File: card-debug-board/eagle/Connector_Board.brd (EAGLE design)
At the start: 65.5 x 34.3 mm, 37 parts, among them J1 ORESAT-DEBUG-CONNECTOR-CARD, J3 USB_A_SMT_FEMALE, Q1 MOSFET-PCH-SOT23-6, U1 FT230XS-R

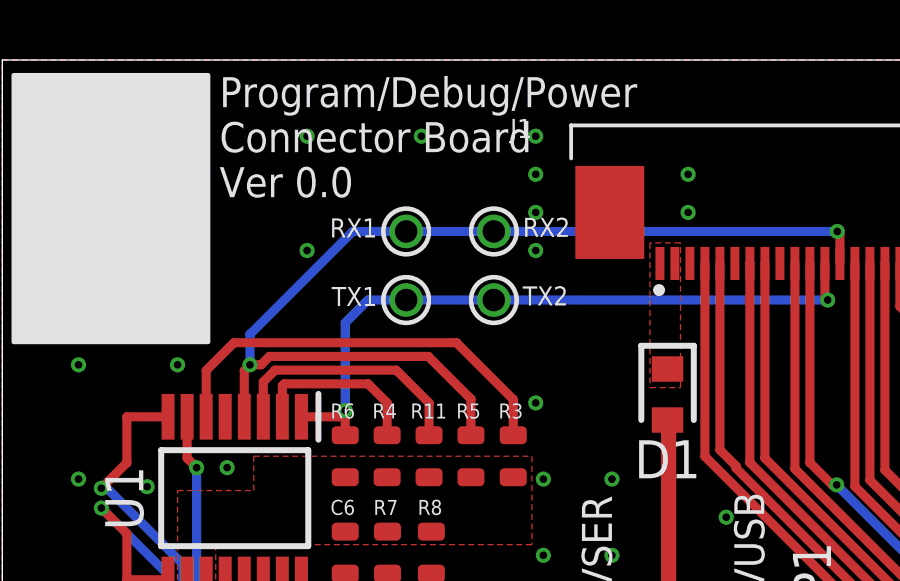
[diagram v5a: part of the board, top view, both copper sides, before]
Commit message: updated the pin connectors
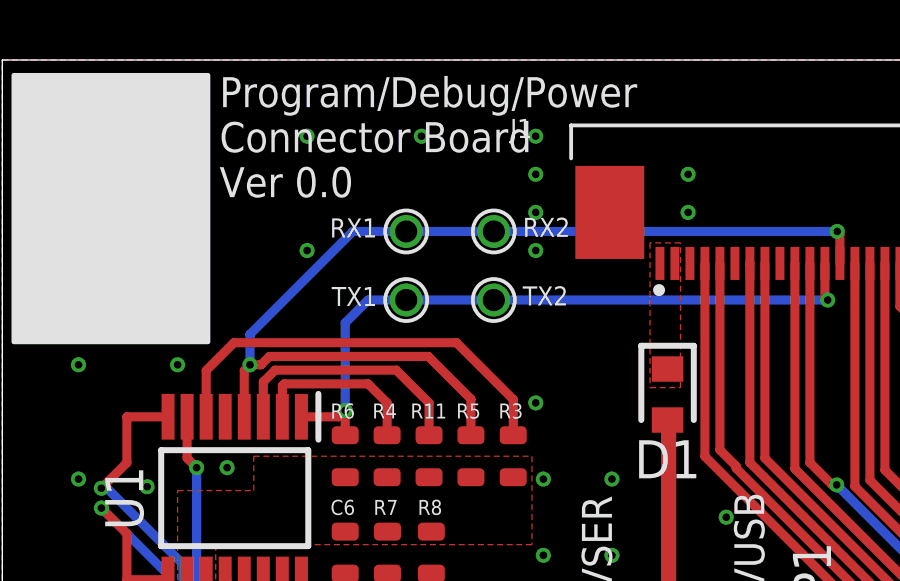
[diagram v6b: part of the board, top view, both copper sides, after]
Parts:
- RX1, RX2, TX1, TX2: value (none) -> TEST-POINT-LARGE; device oresat-misc:TP -> oresat-misc:1X01
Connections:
- net RXD: now also RX1.1, RX2.1; no longer RX1.TP, RX2.TP
- net TXD: now also TX1.1, TX2.1; no longer TX1.TP, TX2.TP
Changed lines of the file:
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@@
 <drawing>
 <settings>
-<setting alwaysvectorfont="yes"/>
+<setting alwaysvectorfont="no"/>
 <setting verticaltext="up"/>
 </settings>
@@
 <layer number="136" name="silktop" color="7" fill="1" visible="yes" active="yes"/>
 <layer number="137" name="silkbottom" color="7" fill="1" visible="yes" active="yes"/>
+<layer number="138" name="mbTest" color="7" fill="1" visible="yes" active="yes"/>
+<layer number="139" name="mtKeepout" color="7" fill="1" visible="yes" active="yes"/>
 <layer number="140" name="Testjig_Mill" color="26" fill="1" visible="yes" active="yes"/>
+<layer number="141" name="mtRestrict" color="7" fill="1" visible="yes" active="yes"/>
+<layer number="142" name="mbRestrict" color="7" fill="1" visible="yes" active="yes"/>
+<layer number="143" name="mvRestrict" color="7" fill="1" visible="yes" active="yes"/>
 <layer number="144" name="Drill_legend" color="7" fill="1" visible="yes" active="yes"/>
 <layer number="145" name="DrillLegend_01-16" color="7" fill="1" visible="yes" active="yes"/>
 <layer number="146" name="DrillLegend_01-20" color="7" fill="1" visible="yes" active="yes"/>
+<layer number="147" name="mMeasures" color="7" fill="1" visible="yes" active="yes"/>
+<layer number="148" name="mDocument" color="7" fill="1" visible="yes" active="yes"/>
+<layer number="149" name="mReference" color="7" fill="1" visible="yes" active="yes"/>
 <layer number="150" name="Notes" color="7" fill="1" visible="yes" active="yes"/>
 <layer number="151" name="HeatSink" color="7" fill="1" visible="yes" active="yes"/>
@@
 <layer number="154" name="FabDoc2" color="7" fill="1" visible="yes" active="yes"/>
 <layer number="155" name="FabDoc3" color="7" fill="1" visible="yes" active="yes"/>
+<layer number="191" name="mNets" color="7" fill="1" visible="yes" active="yes"/>
+<layer number="192" name="mBusses" color="7" fill="1" visible="yes" active="yes"/>
+<layer number="193" name="mPins" color="7" fill="1" visible="yes" active="yes"/>
+<layer number="194" name="mSymbols" color="7" fill="1" visible="yes" active="yes"/>
+<layer number="195" name="mNames" color="7" fill="1" visible="yes" active="yes"/>
+<layer number="196" name="mValues" color="7" fill="1" visible="yes" active="yes"/>
 <layer number="199" name="Contour" color="7" fill="1" visible="yes" active="yes"/>
 <layer number="200" name="200bmp" color="7" fill="1" visible="yes" active="yes"/>
@@
 <attribute name="VALUE" x="12.674" y="22.082" size="0.8" layer="27" font="vector" ratio="15" rot="R270"/>
 </element>
-<element name="RX1" library="oresat-misc" package="TP" package3d_urn="urn:adsk.eagle:package:27946/1" value="" x="13.462" y="28.575" smashed="yes">
+<element name="RX1" library="oresat-misc" package="1X01" value="TEST-POINT-LARGE" x="13.462" y="28.575" smashed="yes">
 <attribute name="NAME" x="12.496" y="29.01" size="0.635" layer="25" font="vector" ratio="20" rot="R180"/>
-<attribute name="POPULARITY" value="12" x="13.462" y="28.575" size="1" layer="27" display="off"/>
-<attribute name="VALUE" value="" x="13.462" y="28.575" size="0.0254" layer="27"/>
-</element>
-<element name="RX2" library="oresat-misc" package="TP" package3d_urn="urn:adsk.eagle:package:27946/1" value="" x="16.383" y="28.575" smashed="yes">
+</element>
+<element name="RX2" library="oresat-misc" package="1X01" value="TEST-POINT-LARGE" x="16.383" y="28.575" smashed="yes">
 <attribute name="NAME" x="17.349" y="28.394" size="0.635" layer="25" font="vector" ratio="20"/>
-<attribute name="POPULARITY" value="12" x="16.383" y="28.575" size="1" layer="27" display="off"/>
-<attribute name="VALUE" value="" x="16.383" y="28.575" size="0.0254" layer="27"/>
-</element>
-<element name="TX1" library="oresat-misc" package="TP" package3d_urn="urn:adsk.eagle:package:27946/1" value="" x="13.462" y="26.289" smashed="yes">
+</element>
+<element name="TX1" library="oresat-misc" package="1X01" value="TEST-POINT-LARGE" x="13.462" y="26.289" smashed="yes">
 <attribute name="NAME" x="12.496" y="26.724" size="0.635" layer="25" font="vector" ratio="20" rot="R180"/>
-<attribute name="POPULARITY" value="12" x="13.462" y="26.289" size="1" layer="27" display="off"/>
-<attribute name="VALUE" value="" x="13.462" y="26.289" size="0.0254" layer="27"/>
-</element>
-<element name="TX2" library="oresat-misc" package="TP" package3d_urn="urn:adsk.eagle:package:27946/1" value="" x="16.383" y="26.289" smashed="yes">
+</element>
+<element name="TX2" library="oresat-misc" package="1X01" value="TEST-POINT-LARGE" x="16.383" y="26.289" smashed="yes">
 <attribute name="NAME" x="17.349" y="26.108" size="0.635" layer="25" font="vector" ratio="20"/>
-<attribute name="POPULARITY" value="12" x="16.383" y="26.289" size="1" layer="27" display="off"/>
-<attribute name="VALUE" value="" x="16.383" y="26.289" size="0.0254" layer="27"/>
 </element>
 </elements>
@@
 <contactref element="U1" pad="1"/>
 <contactref element="R6" pad="1"/>
-<contactref element="TX1" pad="TP"/>
-<contactref element="TX2" pad="TP"/>
+<contactref element="TX1" pad="1"/>
+<contactref element="TX2" pad="1"/>
 <wire x1="9.969" y1="22.397" x2="11.221" y2="22.397" width="0.3048" layer="1"/>
 <wire x1="11.221" y1="22.397" x2="11.43" y2="22.606" width="0.3048" layer="1"/>
@@
 <contactref element="U1" pad="4"/>
 <contactref element="R5" pad="1"/>
-<contactref element="RX1" pad="TP"/>
-<contactref element="RX2" pad="TP"/>
+<contactref element="RX1" pad="1"/>
+<contactref element="RX2" pad="1"/>
 <wire x1="8.065" y1="22.397" x2="8.065" y2="23.94" width="0.3048" layer="1"/>
 <wire x1="8.065" y1="23.94" x2="8.255" y2="24.13" width="0.3048" layer="1"/>

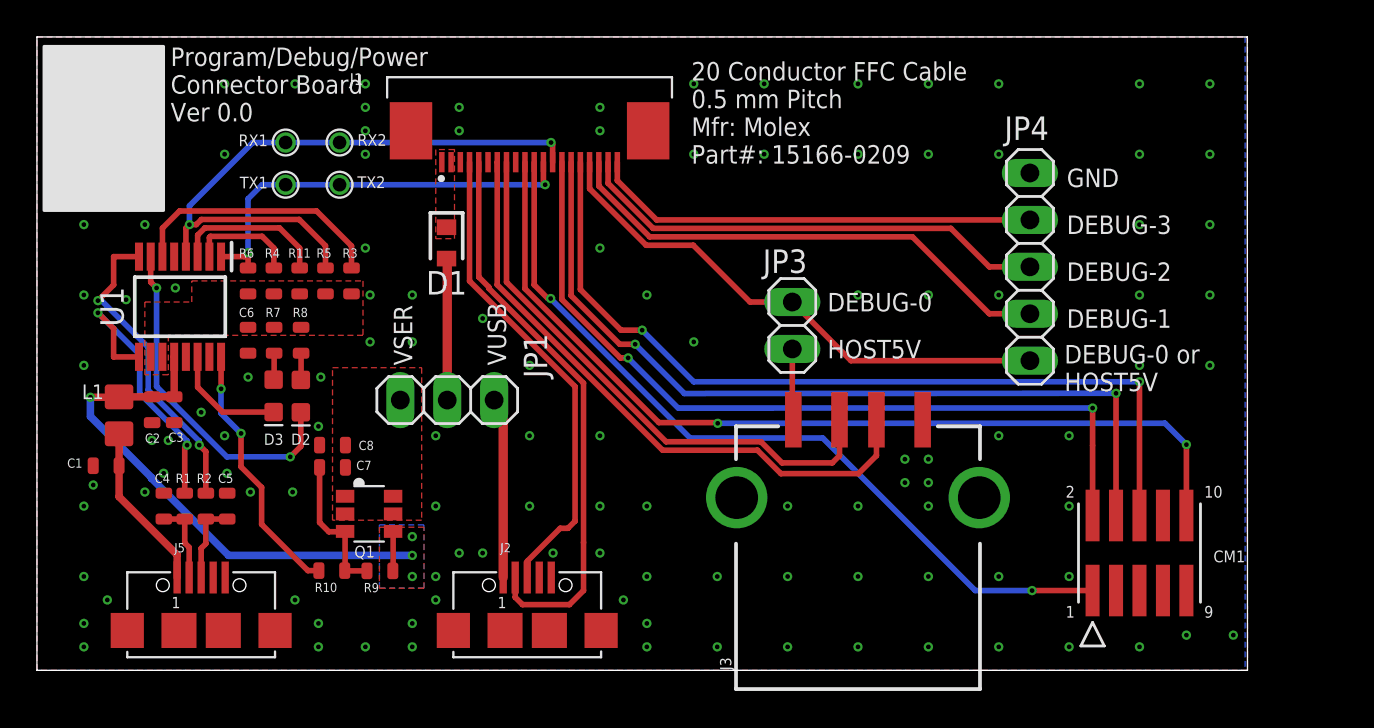
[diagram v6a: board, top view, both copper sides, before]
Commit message: Version 1 of the OreSat debug board. Tinyified the board, added curved corners, centered FFC connector, added reset switch, made USB traces have a continuous ground plane, fixed FT203x VCCIO connection, made USB device shields not connected to ground as per spec, cleaned up silk screen.
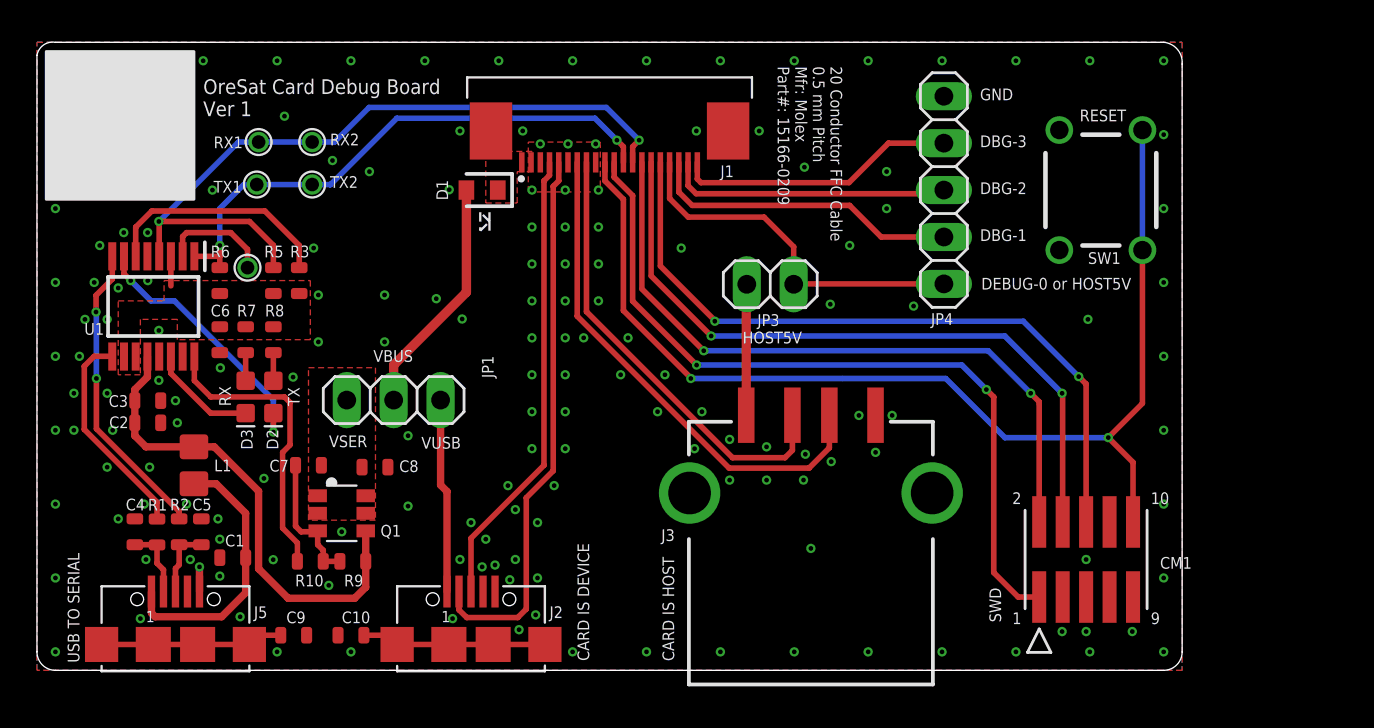
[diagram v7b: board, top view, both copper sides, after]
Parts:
- removed R11, R4: 10k, oresat-rcl:.0603-C-NOSILK
- added !RTS: TEST-POINT-LARGE, oresat-misc:1X01
- added C10, C9: 100nF, oresat-rcl:.0603-C-NOSILK
- added SW1: B3F-1000, apdm_ap_v2:SW-MOM-OMRON-6X6X4.3
- moved C1 8.47 mm to (10.6, 6.10)
- moved JP4 6.24 mm to (49.1, 26.0)
- moved L1 4.87 mm to (8.50, 11.1)
- moved J1 4.33 mm to (31.0, 29.2)
- moved D1 3.45 mm to (24.1, 26.0), turned to 180 degrees
- moved J2 3.14 mm to (23.5, 1.40)
- moved CM1 2.91 mm to (56.8, 6.00)
- moved JP1 2.90 mm to (19.3, 14.6)
- moved R3 2.83 mm to (14.2, 21.1)
- moved R5 2.82 mm to (12.8, 21.1)
- moved C8 2.59 mm to (18.3, 11.0), turned to 0 degrees
- moved J3 2.56 mm to (41.9, 6.60)
- moved JP3 2.53 mm to (39.7, 20.9), turned to 0 degrees
- moved C4 2.10 mm to (5.30, 7.50)
- moved R1 2.05 mm to (6.50, 7.49)
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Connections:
- removed net VCCIO: R11.1, U1.3
- removed net VCCIO_P: C6.1, R11.2, R3.2, R4.2, R5.2, R6.2, R7.2, R8.2, U1.10, U1.11
- new net 3V3OUT: C6.1, R3.2, R5.2, R6.2, R7.2, R8.2, U1.10, U1.11, U1.3
- new net N$1: C9.1, J5.SHELL, J5.SHELL1, J5.SHELL2, J5.SHELL3
- new net N$6: C10.1, J2.SHELL, J2.SHELL1, J2.SHELL2, J2.SHELL3
- net GND: now also C10.2, C9.2, SW1.3, SW1.4; no longer J2.SHELL, J2.SHELL1, J2.SHELL2, J2.SHELL3, J5.SHELL, J5.SHELL1, J5.SHELL2, J5.SHELL3
- net NRST: now also SW1.1, SW1.2
- net RTS#: now also !RTS.1; no longer R4.1
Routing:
- net DEBUG-1: track 27.5 -> 17.0 mm
- net DEBUG-2: track 25.9 -> 15.4 mm
- net NRST: track 50.0 -> 60.1 mm
- net N$6: track 0.00 -> 10.0 mm
- net N$1: track 0.00 -> 9.91 mm
- net DEBUG-0/HOST5V: track 29.1 -> 19.9 mm
- net DEBUG-3: track 24.2 -> 15.2 mm
- net VCCIO: track 8.38 -> 0.00 mm
- net SWO: track 46.5 -> 38.8 mm
- net SWCLK: track 45.5 -> 38.0 mm
- net SWDIO: track 44.4 -> 37.4 mm
- net TXD: track 23.0 -> 30.0 mm
- net RXD: track 34.2 -> 40.5 mm
- net HOSTD_P: track 33.7 -> 27.6 mm
- net HOSTD_N: track 30.7 -> 24.6 mm
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- added copper zone on layer 1, net 3V3OUT
- removed copper zone on layer 1, net VCC
- removed copper zone on layer 16, net VCC
- removed copper zone on layer 1, net VCCIO_P
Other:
- board size 65.5 x 34.3 mm -> 62 x 34 mm
- board text added: "CARD IS DEVICE"
- board text added: "CARD IS HOST"
- board text added: "Connector Clearance"
- board text added: "DBG-1"
- board text added: "DBG-2"
- board text added: "DBG-3"
- board text added: "OreSat Card Debug Board Ver 1"
- board text added: "RESET"
- board text added: "RX"
- board text added: "SWD"
- board text added: "TX"
- board text added: "USB TO SERIAL"
- board text added: "VBUS"
- board text removed: "DEBUG-0"
- board text removed: "DEBUG-1"
- board text removed: "DEBUG-2"
- board text removed: "DEBUG-3"
- board text removed: "Program/Debug/Power Connector Board Ver 0.0"

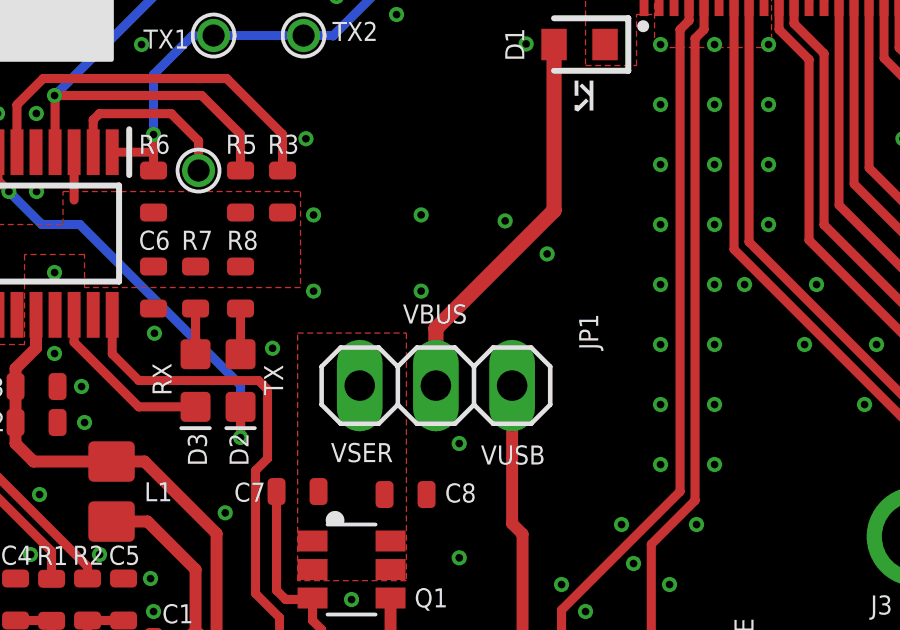
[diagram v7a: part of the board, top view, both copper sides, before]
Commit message: Renamed VBUS to VBUSP added attributes to make BOM
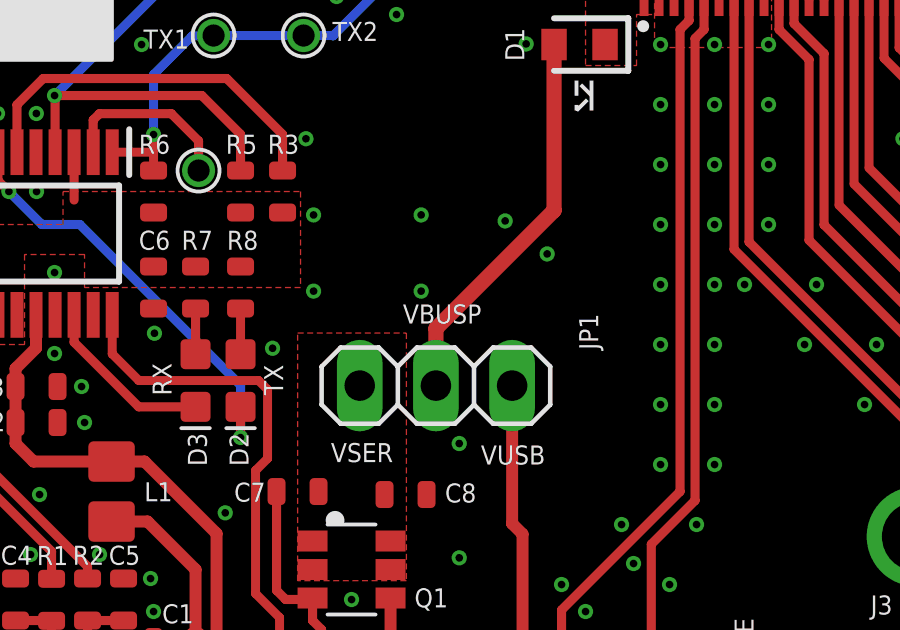
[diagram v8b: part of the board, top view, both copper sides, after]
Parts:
- C10, C3, C6, C7, C8, C9: value 100nF -> .1u
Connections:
- net VBUS renamed VBUSP
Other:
- board text added: "VBUSP"
- board text removed: "VBUS"
